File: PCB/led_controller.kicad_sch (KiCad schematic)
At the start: 29 parts, among them U1 LM339, U3 LM339

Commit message: add footprints for power supply
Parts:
- added TP1: TestPoint, TestPoint:TestPoint_Keystone_5000-5004_Miniature, symbol Connector:TestPoint
- R10, R4, R5, R6, R7, R8, R9: value R -> 2k; footprint (none) -> Resistor_SMD:R_0805_2012Metric_Pad1.20x1.40mm_HandSolder
- R11, R12, R13, R14, R15, R16, R17, R18, R2, R3: footprint (none) -> Resistor_SMD:R_0805_2012Metric_Pad1.20x1.40mm_HandSolder
- U1: footprint (none) -> Package_SO:SO-14_3.9x8.65mm_P1.27mm; link (none) -> https://www.tme.eu/de/details/lm339dt/smd-komparatoren/stmi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
- U3: footprint Package_DIP:DIP-8_W7.62mm -> Package_SO:SO-14_3.9x8.65mm_P1.27mm
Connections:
- net signal_amp_in: now also TP1.1
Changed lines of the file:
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@@
 	)
 	(junction
+		(at 85.09 171.45)
+		(diameter 0)
+		(color 0 0 0 0)
+	)
+	(junction
 		(at 134.62 59.69)
 		(diameter 0)
@@
 	(wire
 		(pts
-			(xy 100.33 171.45) (xy 77.47 171.45)
+			(xy 100.33 171.45) (xy 85.09 171.45)
 		)
 		(stroke
@@
 	(wire
 		(pts
+			(xy 85.09 171.45) (xy 77.47 171.45)
+		)
+		(stroke
+			(width 0)
+			(type default)
+		)
+	)
+	(wire
+		(pts
 			(xy 161.29 115.57) (xy 161.29 128.27)
 		)
@@
 			)
 		)
-		(property "Footprint" ""
+		(property "Footprint" "Resistor_SMD:R_0805_2012Metric_Pad1.20x1.40mm_HandSolder"
 			(at 144.78 74.168 90)
 			(hide yes)
@@
 			)
 		)
-		(property "Footprint" ""
+		(property "Footprint" "Resistor_SMD:R_0805_2012Metric_Pad1.20x1.40mm_HandSolder"
 			(at 144.78 130.048 90)
 			(hide yes)
@@
 			)
 		)
-		(property "Footprint" ""
+		(property "Footprint" "Resistor_SMD:R_0805_2012Metric_Pad1.20x1.40mm_HandSolder"
 			(at 62.992 175.26 90)
 			(hide yes)
@@
 			)
 		)
-		(property "Footprint" ""
+		(property "Footprint" "Package_SO:SO-14_3.9x8.65mm_P1.27mm"
 			(at 91.44 113.03 0)
 			(hide yes)
@@
 			)
 		)
+		(property "link" "https://www.tme.eu/de/details/lm339dt/smd-komparatoren/stmicroelectronics/"
+			(at 92.71 115.57 0)
+			(hide yes)
+			(show_name no)
+			(do_not_autoplace no)
+			(effects
+				(font
+					(size 1.27 1.27)
+				)
+			)
+		)
 		(pin "4"
 		)
@@
 			)
 		)
-		(property "Footprint" ""
+		(property "Footprint" "Package_SO:SO-14_3.9x8.65mm_P1.27mm"
 			(at 231.14 92.71 0)
 			(hide yes)
@@
 			)
 		)
+		(property "link" "https://www.tme.eu/de/details/lm339dt/smd-komparatoren/stmicroelectronics/"
+			(at 232.41 95.25 0)
+			(hide yes)
+			(show_name no)
+			(do_not_autoplace no)
+			(effects
+				(font
+					(size 1.27 1.27)
+				)
+			)
+		)
 		(pin "4"
 		)
@@
 			)
 		)
-		(property "Footprint" "Package_DIP:DIP-8_W7.62mm"
+		(property "Footprint" "Package_SO:SO-14_3.9x8.65mm_P1.27mm"
 			(at 91.44 57.15 0)
 			(hide yes)
@@
 			)
 		)
-		(property "Footprint" "Package_DIP:DIP-8_W7.62mm"
+		(property "Footprint" "Package_SO:SO-14_3.9x8.65mm_P1.27mm"
 			(at 101.6 97.79 0)
 			(hide yes)
@@
 			)
 		)
-		(property "Value" "R"
+		(property "Value" "2k"
 			(at 67.31 92.7099 0)
 			(show_name no)
@@
 			)
 		)
-		(property "Footprint" ""
+		(property "Footprint" "Resistor_SMD:R_0805_2012Metric_Pad1.20x1.40mm_HandSolder"
 			(at 62.992 91.44 90)
 			(hide yes)
@@
 			)
 		)
-		(property "Footprint" ""
+		(property "Footprint" "Package_SO:SO-14_3.9x8.65mm_P1.27mm"
 			(at 91.44 140.97 0)
 			(hide yes)
@@
 			)
 		)
+		(property "link" "https://www.tme.eu/de/details/lm339dt/smd-komparatoren/stmicroelectronics/"
+			(at 92.71 143.51 0)
+			(hide yes)
+			(show_name no)
+			(do_not_autoplace no)
+			(effects
+				(font
+					(size 1.27 1.27)
+				)
+			)
+		)
 		(pin "4"
 		)
@@
 			)
 		)
-		(property "Footprint" ""
+		(property "Footprint" "Resistor_SMD:R_0805_2012Metric_Pad1.20x1.40mm_HandSolder"
 			(at 144.78 89.408 90)
 			(hide yes)
@@
 			)
 		)
-		(property "Footprint" ""
+		(property "Footprint" "Resistor_SMD:R_0805_2012Metric_Pad1.20x1.40mm_HandSolder"
 			(at 144.78 117.348 90)
 			(hide yes)
@@
 			)
 		)
-		(property "Footprint" ""
+		(property "Footprint" "Package_SO:SO-14_3.9x8.65mm_P1.27mm"
 			(at 101.6 125.73 0)
 			(hide yes)
@@
 			)
 		)
+		(property "link" "https://www.tme.eu/de/details/lm339dt/smd-komparatoren/stmicroelectronics/"
+			(at 102.87 128.27 0)
+			(hide yes)
+			(show_name no)
+			(do_not_autoplace no)
+			(effects
+				(font
+					(size 1.27 1.27)
+				)
+			)
+		)
 		(pin "4"
 		)
@@
 	)
 	(symbol
+		(lib_id "Connector:TestPoint")
+		(at 85.09 171.45 0)
+		(unit 1)
+		(body_style 1)
+		(exclude_from_sim no)
+		(in_bom yes)
+		(on_board yes)
+		(in_pos_files yes)
+		(dnp no)
+		(fields_autoplaced yes)
+		(property "Reference" "TP1"
+			(at 87.63 166.8779 0)
+			(show_name no)
+			(do_not_autoplace no)
+			(effects
+				(font
+					(size 1.27 1.27)
+				)
+				(justify left)
+			)
+		)
+		(property "Value" "TestPoint"
+			(at 87.63 169.4179 0)
+			(show_name no)
+			(do_not_autoplace no)
+			(effects
+				(font
+					(size 1.27 1.27)
+				)
+				(justify left)
+			)
+		)
+		(property "Footprint" "TestPoint:TestPoint_Keystone_5000-5004_Miniature"
+			(at 90.17 171.45 0)
+			(hide yes)
+			(show_name no)
+			(do_not_autoplace no)
+			(effects
+				(font
+					(size 1.27 1.27)
+				)
+			)
+		)
+		(property "Datasheet" ""
+			(at 90.17 171.45 0)
+			(hide yes)
+			(show_name no)
+			(do_not_autoplace no)
+			(effects
+				(font
+					(size 1.27 1.27)
+				)
+			)
+		)
+		(property "Description" "test point"
+			(at 85.09 171.45 0)
+			(hide yes)
+			(show_name no)
+			(do_not_autoplace no)
+			(effects
+				(font
+					(size 1.27 1.27)
+				)
+			)
+		)
+		(pin "1"
+		)
+		(instances
+			(project "UV_badge"
+				(path "/510c3167-274e-48e8-bc0f-ce517acc7f9d/c13bce2c-c64f-4126-ad9a-b7d870433f01"
+					(reference "TP1")
+					(unit 1)
+				)
+			)
+		)
+	)
+	(symbol
 		(lib_id "power:+5V")
 		(at 161.29 49.53 0)
@@
 			)
 		)
-		(property "Footprint" ""
+		(property "Footprint" "Resistor_SMD:R_0805_2012Metric_Pad1.20x1.40mm_HandSolder"
 			(at 144.78 102.108 90)
 			(hide yes)
@@
 			)
 		)
-		(property "Value" "R"
+		(property "Value" "2k"
 			(at 67.31 63.4999 0)
 			(show_name no)
@@
 			)
 		)
-		(property "Footprint" ""
+		(property "Footprint" "Resistor_SMD:R_0805_2012Metric_Pad1.20x1.40mm_HandSolder"
 			(at 62.992 62.23 90)
 			(hide yes)
@@
 			)
 		)
-		(property "Footprint" "Package_DIP:DIP-8_W7.62mm"
+		(property "Footprint" "Package_SO:SO-14_3.9x8.65mm_P1.27mm"
 			(at 91.44 85.09 0)
 			(hide yes)
@@
 			)
 		)
-		(property "Value" "R"
+		(property "Value" "2k"
 			(at 67.31 106.6799 0)
 			(show_name no)
@@
 			)
 		)
-		(property "Footprint" ""
+		(property "Footprint" "Resistor_SMD:R_0805_2012Metric_Pad1.20x1.40mm_HandSolder"
 			(at 62.992 105.41 90)
 			(hide yes)
@@
 			)
 		)
-		(property "Value" "R"
+		(property "Value" "2k"
 			(at 67.31 78.7399 0)
 			(show_name no)
@@
 			)
 		)
-		(property "Footprint" ""
+		(property "Footprint" "Resistor_SMD:R_0805_2012Metric_Pad1.20x1.40mm_HandSolder"
 			(at 62.992 77.47 90)
 			(hide yes)
@@
 			)
 		)
-		(property "Footprint" ""
+		(property "Footprint" "Package_SO:SO-14_3.9x8.65mm_P1.27mm"
 			(at 101.6 153.67 0)
 			(hide yes)
@@
 			)
 		)
+		(property "link" "https://www.tme.eu/de/details/lm339dt/smd-komparatoren/stmicroelectronics/"
+			(at 102.87 156.21 0)
+			(hide yes)
+			(show_name no)
+			(do_not_autoplace no)
+			(effects
+				(font
+					(size 1.27 1.27)
+				)
+			)
+		)
 		(pin "4"
 		)
@@
 			)
 		)
-		(property "Footprint" ""
+		(property "Footprint" "Resistor_SMD:R_0805_2012Metric_Pad1.20x1.40mm_HandSolder"
 			(at 144.78 61.468 90)
 			(hide yes)
@@
 			)
 		)
-		(property "Footprint" "Package_DIP:DIP-8_W7.62mm"
+		(property "Footprint" "Package_SO:SO-14_3.9x8.65mm_P1.27mm"
 			(at 219.71 92.71 0)
 			(hide yes)
@@
 			)
 		)
-		(property "Value" "R"
+		(property "Value" "2k"
 			(at 67.31 147.3199 0)
 			(show_name no)
@@
 			)
 		)
-		(property "Footprint" ""
+		(property "Footprint" "Resistor_SMD:R_0805_2012Metric_Pad1.20x1.40mm_HandSolder"
 			(at 62.992 146.05 90)
 			(hide yes)
@@
 			)
 		)
-		(property "Footprint" ""
+		(property "Footprint" "Resistor_SMD:R_0805_2012Metric_Pad1.20x1.40mm_HandSolder"
 			(at 62.992 39.37 90)
 			(hide yes)
@@
 			)
 		)
-		(property "Footprint" ""
+		(property "Footprint" "Resistor_SMD:R_0805_2012Metric_Pad1.20x1.40mm_HandSolder"
 			(at 144.78 157.988 90)
 			(hide yes)
@@
 			)
 		)
-		(property "Footprint" "Package_DIP:DIP-8_W7.62mm"
+		(property "Footprint" "Package_SO:SO-14_3.9x8.65mm_P1.27mm"
 			(at 101.6 69.85 0)
 			(hide yes)
@@
 			)
 		)
-		(property "Value" "R"
+		(property "Value" "2k"
 			(at 67.31 120.6499 0)
 			(show_name no)
@@
 			)
 		)
-		(property "Footprint" ""
+		(property "Footprint" "Resistor_SMD:R_0805_2012Metric_Pad1.20x1.40mm_HandSolder"
 			(at 62.992 119.38 90)
 			(hide yes)
@@
 			)
 		)
-		(property "Value" "R"
+		(property "Value" "2k"
 			(at 67.31 134.6199 0)
 			(show_name no)
@@
 			)
 		)
-		(property "Footprint" ""
+		(property "Footprint" "Resistor_SMD:R_0805_2012Metric_Pad1.20x1.40mm_HandSolder"
 			(at 62.992 133.35 90)
 			(hide yes)
@@
 			)
 		)
-		(property "Footprint" ""
+		(property "Footprint" "Resistor_SMD:R_0805_2012Metric_Pad1.20x1.40mm_HandSolder"
 			(at 144.78 145.288 90)
 			(hide yes)

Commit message: add missing symbols
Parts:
- RV1, RV2: footprint Potentiometer_THT:Potentiometer_Runtron_RM-065_Vertical -> Potentiometer_SMD:Potentiometer_Bourns_TC33X_Vertical
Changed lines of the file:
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@@
 			)
 		)
-		(property "Footprint" "Potentiometer_THT:Potentiometer_Runtron_RM-065_Vertical"
+		(property "Footprint" "Potentiometer_SMD:Potentiometer_Bourns_TC33X_Vertical"
 			(at 64.77 163.83 0)
 			(hide yes)
@@
 			)
 		)
-		(property "Description" "Trim-potentiometer"
+		(property "Description" "https://de.aliexpress.com/item/1005011873525568.html?spm=a2g0o.productlist.main.11.3fd718e5mXjZiQ&algo_pvid=7613c848-f431-45d5-941b-d2d154c92b7a&algo_exp_id=7613c848-f431-45d5-941b-d2d154c92b7a-10&pdp_ext_f=%7B%22order%22%3A%2243%22%2C%22spu_best_type%22%3A%22price%22%2C%22eval%22%3A%221%22%2C%22fromPage%22%3A%22search%22%7D&pdp_npi=6%40dis%21EUR%216.49%213.05%21%21%2147.55%2122.35%21%400b5e1a3817922524457713019e0d45%2112000056846451159%21sea%21DE%216126981087%21X%211%210%21n_tag%3A-29919%3Bd%3A55183b53%3Bm03_new_user%3A-29895&curPageLogUid=OkjEOPcjFXqP&utparam-url=scene%3Asearch%7Cquery_from%3A%7Cx_object_id%3A1005011873525568%7C_p_origin_prod%3A"
 			(at 64.77 163.83 0)
 			(hide yes)
@@
 			)
 		)
-		(property "Footprint" "Potentiometer_THT:Potentiometer_Runtron_RM-065_Vertical"
+		(property "Footprint" "Potentiometer_SMD:Potentiometer_Bourns_TC33X_Vertical"
 			(at 64.77 50.8 0)
 			(hide yes)

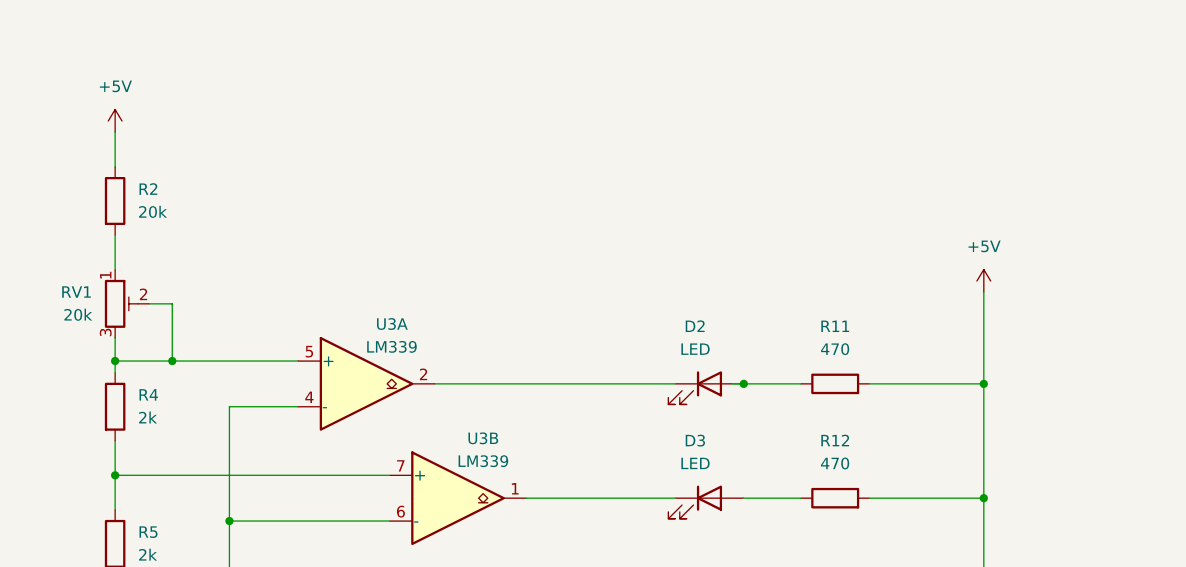
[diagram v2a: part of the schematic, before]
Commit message: update LED footprint reverse mount
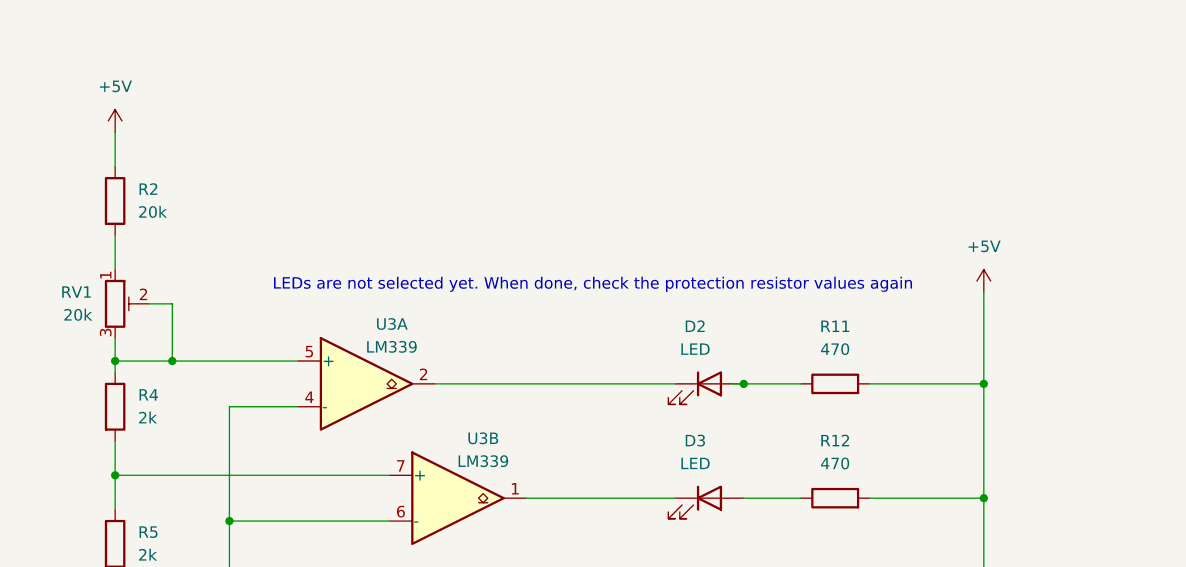
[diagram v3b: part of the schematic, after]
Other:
- note added: "LEDs are not selected yet. When done, check the protection resistor values again"
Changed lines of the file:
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@@
+		)
+	)
+	(text "LEDs are not selected yet. When done, check the protection resistor values again"
+		(exclude_from_sim no)
+		(at 117.856 48.768 0)
+		(effects
+			(font
+				(size 1.27 1.27)
+			)
 		)
 	)

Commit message: component distributions
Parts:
- D2, D3, D4, D5, D6, D7, D8, D9: footprint LED_SMD:LED_Cree-XHP50_3V_HighDensity -> Library_local:LED_1206_3216Metric_ReverseMount
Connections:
- net +5V: now also D2.2 (A), D3.2 (A), D4.2 (A), D5.2 (A), D6.2 (A), D7.2 (A), D8.2 (A), D9.2 (A); no longer R11.2, R12.2, R13.2, R14.2, R15.2, R16.2, R17.2, R18.2
- net at R12.1: now also U3.1; no longer D3.2 (A)
- net at R16.1: now also U1.1; no longer D7.2 (A)
- net at D4.1 (K): now also R13.2; no longer U3.13
- net at R13.1: now also U3.13; no longer D4.2 (A)
- net at U1.2: now also R15.1; no longer D6.1 (K)
- net at U3.2: now also R11.1; no longer D2.1 (K)
- net at D3.1 (K): now also R12.2; no longer U3.1
- net at D5.1 (K): now also R14.2; no longer U3.14
- net at R14.1: now also U3.14; no longer D5.2 (A)
- net at U1.13: now also R17.1; no longer D8.1 (K)
- net at D7.1 (K): now also R16.2; no longer U1.1
- net at D9.1 (K): now also R18.2; no longer U1.14
- net at R18.1: now also U1.14; no longer D9.2 (A)
- new net: D6.1 (K), R15.2
- new net: D2.1 (K), R11.2
- new net: D8.1 (K), R17.2
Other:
- moved on the sheet: D2, D3, D4, D5, D6, D7, D8, D9, R11, R12, R13, R14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
